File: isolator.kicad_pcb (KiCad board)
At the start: 4 copper layers, 120 x 50 mm, 52 parts, among them J1 HOST, J2 ISO_PORT, Q1 2N7002, T1 750313638, U1 ADuM4165, U2 USBLC6-2SC6, U3 USBLC6-2SC6, U4 SN6505BDBV, U5 TLV76750DGNR, U6 TPS2553DBV, Y1 24M 8pF

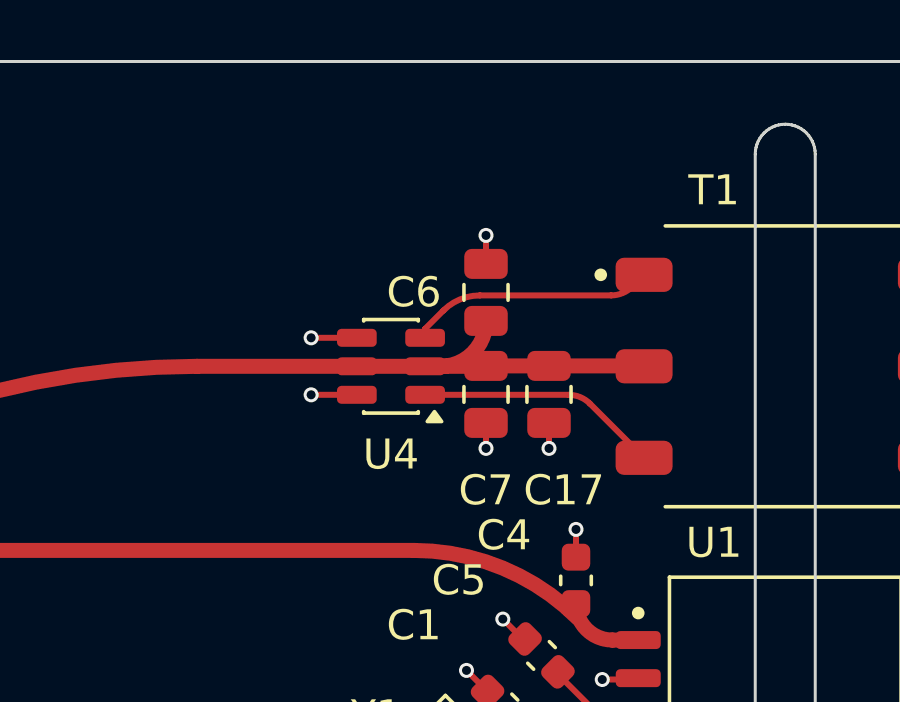
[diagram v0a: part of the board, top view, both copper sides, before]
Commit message: fix(pcb): restore barrier netclass coverage, swap C6/C7 at U4
The schematic label rework renamed thirteen nets out from under the
netclass patterns, which still match the slash-prefixed local-label names
(/VBUS_HOST, /ISO_5V, /PORT_VBUS, /VDD1, /VDD2, /DCDC_*). VBUS_HOST, VDD1,
ISO_5V, PORT_VBUS, VDD2, Net-(D1-K), Net-(D3-A/K), Net-(D4-A/K),
Net-(J2-CC1/CC2) and Net-(U6-ILIM) all fell through to Default, so the
barrier rules in isolator.kicad_dru -- gated on hasNetclass('HOST_SIDE')
&& hasNetclass('ISO_SIDE') -- never fired on them. DRC reported zero
violations because those pairs were never tested, and Gate 1 declined to
run at all rather than report a result it could not trust.

Each net's domain was taken from netlist connectivity, not from its name.
Assigned via netclass_assignments; the patterns themselves still carry the
stale names and no MCP tool edits them. That mechanism holds one class per
net, so VBUS_HOST, ISO_5V, PORT_VBUS and Net-(D1-K) keep their side class
but lose PWR -- which sets defaults for new routing only and does not
touch the copper already laid.

Gate 1 now runs and passes: 8.3000 mm on both inner layers, 11.6834 mm on
B.Cu, 17.6500 mm creepage on F.Cu. DRC is back to zero having actually
evaluated the barrier.

C6 and C7 were transposed against the 2026-08-03 amendment, failing both
the 2.5 mm budget and the C6-inboard rule. Swapped in place rather than to
the spec's coordinates: the spec puts the outboard cap at y 84.150, which
predates /PP_B's route at y 84.500 through the inter-pad channel and would
leave it inside its clearance. Both parts are 0805 on the same two nets, so
the swap leaves every track terminating on the same copper. C6's reference
text followed the footprint onto C17 and moved south.

netclass_coverage.py read only netclass_patterns, so it scored explicit
assignments as unclassified -- the mirror of the hole it exists to catch.
It and barrier.py now resolve both mechanisms.

Still failing, both untouched here: decoupli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
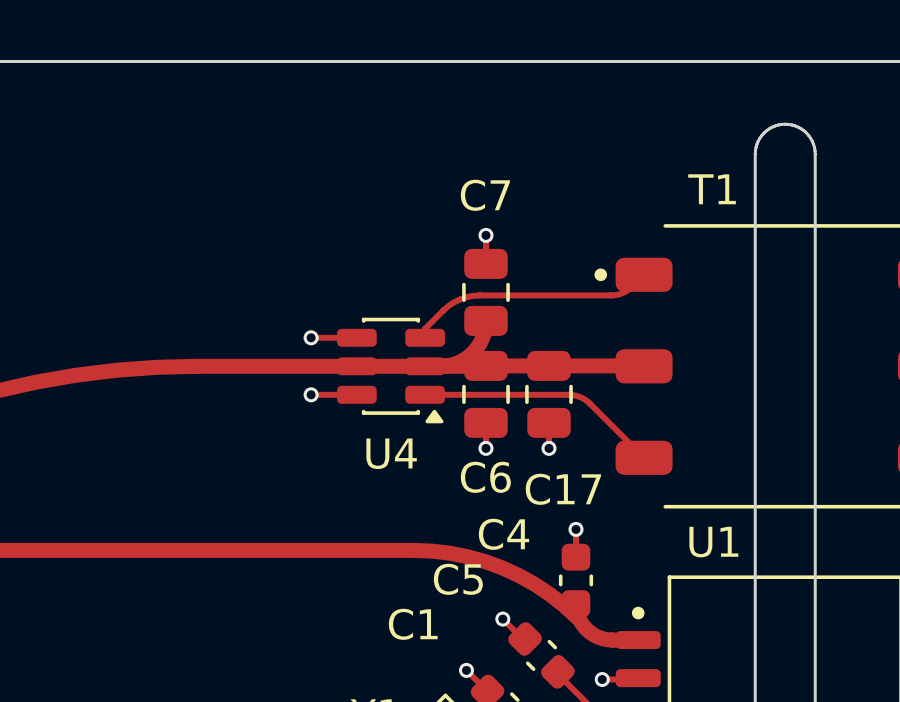
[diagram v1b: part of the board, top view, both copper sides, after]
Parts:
- moved C6 3.40 mm to (136.9, 87.8), turned to -90 degrees
- moved C7 3.40 mm to (136.9, 84.4), turned to 90 degrees

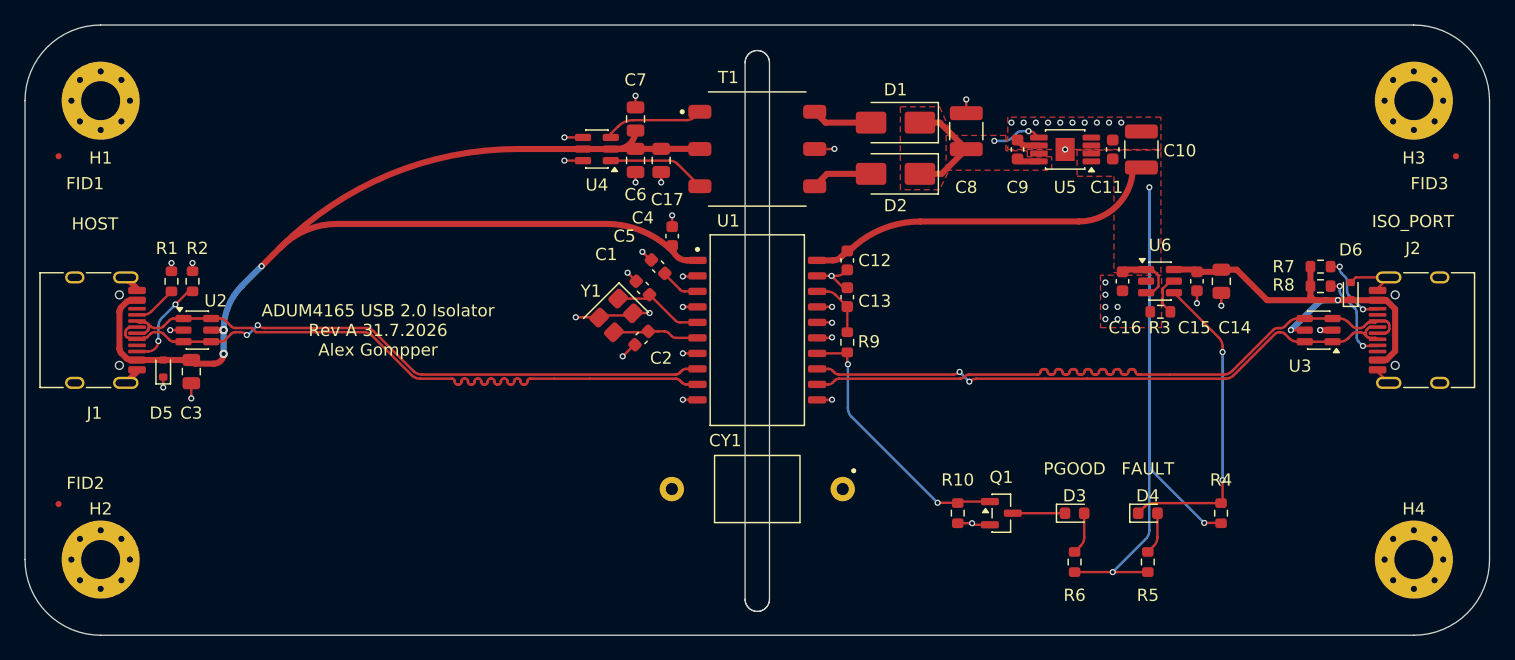
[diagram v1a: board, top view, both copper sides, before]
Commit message: feat(pcb): ground pour on both outer layers, stitched
Four zones, not two: GND1 host-side and GND2 isolated-side on each of F.Cu and
B.Cu. A single pour per outer layer would bridge the barrier, the same reason
the inner layers are split. Outlines are cloned from the GND_SPLIT_A planes so
the 2 mm edge pullback and rounded corners match exactly -- letting the
board-outline clip generate the corners instead would leave outer copper 0.3 mm
from the corner edge, closer than the inner layers, on the two layers that
actually face the extrusion.

Filled: F.Cu 2157.9 mm2 GND1 / 2030.7 mm2 GND2, B.Cu 2434.4 / 2400.4. Island
removal is ALWAYS, so no fill region survives without a connection to its net.

New DRU rule diffpair-pour-gap holds the pour 0.65 mm off both 90 ohm pairs,
about 3x the 0.2104 mm prepreg height. The pairs already reference GND_SPLIT_A
through that prepreg, so outer pour adds only coplanar coupling, which lowers
Zdiff -- and diffpair.py computes Zdiff from w/s/h/Er alone, so it would have
gone on reporting 96.28 ohm for a board that no longer measured it. Verified
against the stored fill rather than trusting the filler: 0.650 mm on F.Cu.

171 stitching vias (86 GND1, 85 GND2) on a 6 mm grid, densified around U4/T1/U1
and U5/U6/U3/D1/D2, placed only inside an existing GND zone so none crosses the
barrier -- max host x 140.875 against the keepout at 142.725. Board total 72 ->
243.

add_gnd_stitching_vias needed cleanup on two counts, now in tools/fix_stitch_drc.py:
its collision check is copper-only and dropped five vias onto existing drills
(worst pair 0.0162 mm hole-to-hole), and its default 2.9 mm edge margin was
needed to keep annuli out of the edge keepout. Ten pads could not form two
thermal spokes -- the USB-C shield grounds at 0.5 mm pitch, U5.4 and C10.2 --
and take a solid zone connection, which is the better answer for a connector
shield and an LDO ground anyway. The pours stay thermal elsewhere so small
passives keep their reflow balance.

deco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
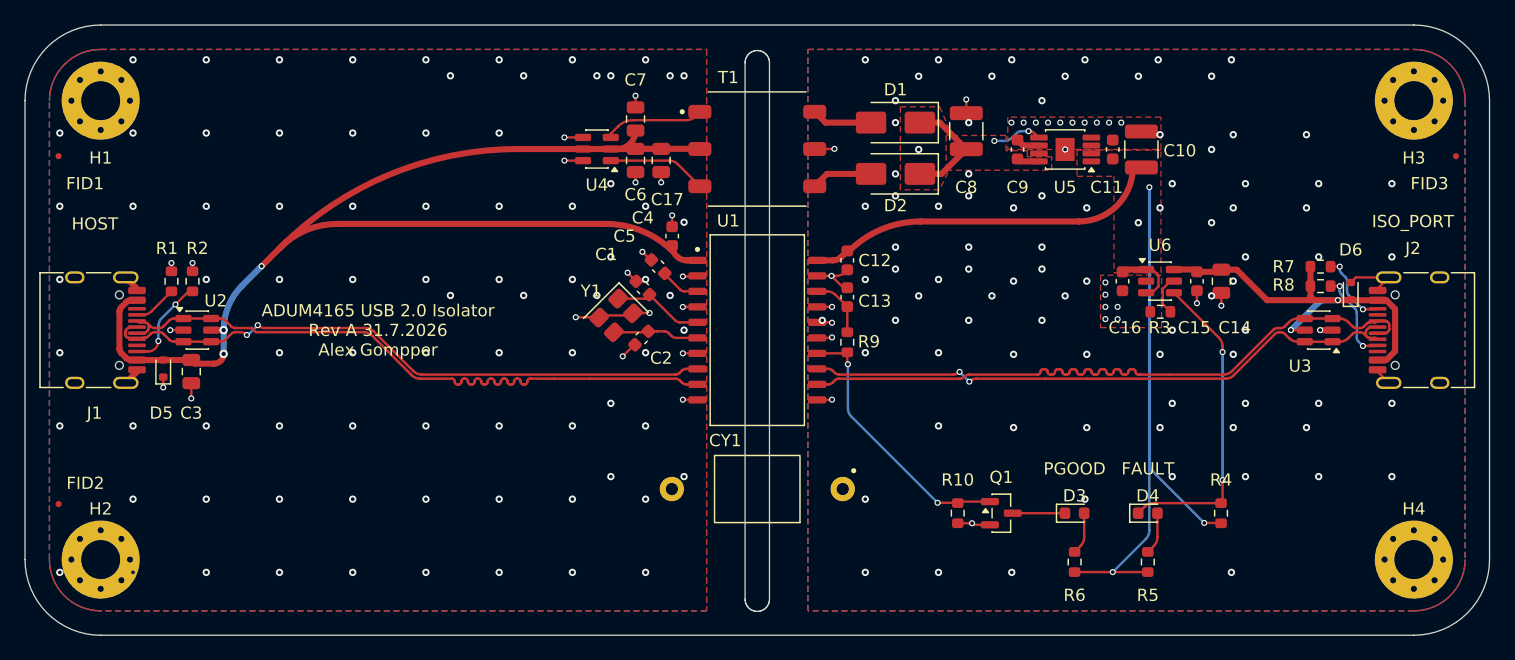
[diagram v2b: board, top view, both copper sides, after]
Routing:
- net GND2: vias 28 -> 116
- net GND1: vias 20 -> 103
- added copper zone on B.Cu, net GND1
- added copper zone on F.Cu, net GND1
- added copper zone on B.Cu, net GND2
